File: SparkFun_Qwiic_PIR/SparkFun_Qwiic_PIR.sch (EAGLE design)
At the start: 39 parts, among them J1 QWIIC_RIGHT_ANGLE, J2 QWIIC_RIGHT_ANGLE, Q1 220mA/50V/3.5Ω, Q2 220mA/50V/3.5Ω, U1 PL-N823-01PL-N823-01_LENS, U2 ADS1015, U3 TPS61200

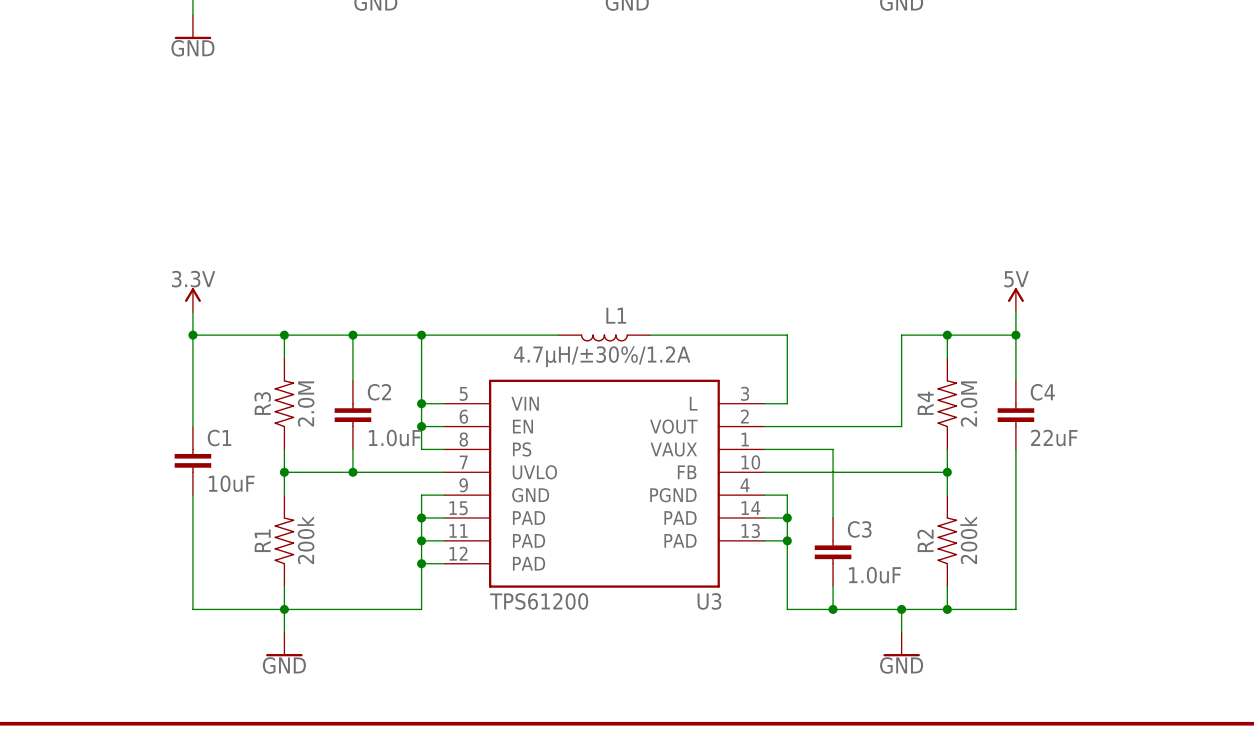
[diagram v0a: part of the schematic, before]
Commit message: Upload 15V revision with LTC3122 Boost IC
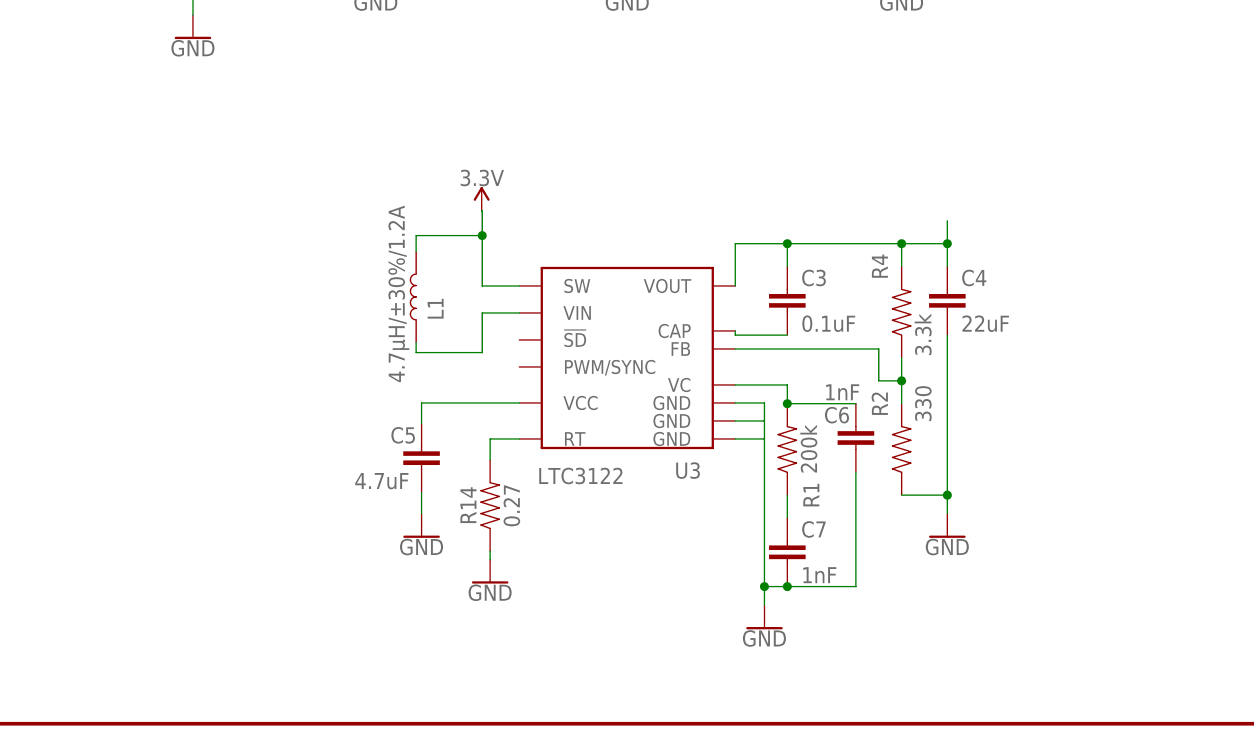
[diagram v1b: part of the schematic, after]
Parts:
- removed C1: 10uF, SparkFun-Capacitors:10UF-0805-10V-10%
- removed C2: 1.0uF, SparkFun-Capacitors:1.0UF-0603-16V-10%
- removed R3: 2.0M, SparkFun-Resistors:2MOHMS-0603-1/10W-1%
- added C5: 4.7uF, SparkFun-Capacitors:4.7UF-1206-16V-(+80/-20%)
- added C6, C7: 1nF, SparkFun-Capacitors:1.0NF/1000PF-0603-50V-10%
- added R14: 0.27, SparkFun-Resistors:0.27OHM-0603-1/10W-1%
- C3: value 1.0uF -> 0.1uF; device SparkFun-Capacitors:1.0UF-0603-16V-10% -> SparkFun-Capacitors:0.1UF-0603-25V-(+80/-20%)
- C4: device SparkFun-Capacitors:22UF-0603-6.3V-20% -> SparkFun-Capacitors:22UF-0805-6.3V-20%
- R2: value 200k -> 330; device SparkFun-Resistors:200KOHM-0603-1/10W-1% -> SparkFun-Resistors:330OHM-0603-1/10W-1%
- R4: value 2.0M -> 3.3k; device SparkFun-Resistors:2MOHMS-0603-1/10W-1% -> SparkFun-Resistors:3.3KOHM-0603-1/10W-1%
- U3: value TPS61200 -> LTC3122; device SparkFun-IC-Power:TPS61200 -> LTC3122:LTC3122
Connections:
- new net N$11: C6.1, R1.2, U3.VC
- new net N$12: C7.1, R1.1
- new net N$5: R14.2, U3.RT
- new net N$6: C3.1, C4.1, R4.2, U3.VOUT
- net 3.3V: now also U3.SW; no longer C1.1, C2.1, R3.2, U3.EN, U3.PS, U3.VIN
- net 5V: no longer C4.1, R4.2, U3.VOUT
- net GND: now also C5.2, C6.2, C7.2, R14.1, U3.GND@1, U3.GND@2; no longer C1.2, C3.2, R1.1, U3.PAD@1, U3.PAD@2, U3.PAD@3, U3.PAD@4, U3.PAD@5, U3.PGND
- net N$1: now also C5.1, U3.VCC; no longer L1.1, U3.L
- net N$3: now also L1.1, U3.VIN; no longer C2.2, R1.2, R3.1, U3.UVLO
- net N$7: now also C3.2, U3.CAP; no longer C3.1, U3.VAUX
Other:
- moved on the sheet: C3, C4, L1, R1, R2, R4
